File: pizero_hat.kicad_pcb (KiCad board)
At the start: 2 copper layers, 65 x 30 mm, 33 parts, among them J1 Raspberry_Pi_2_3, J2 USB_B_Micro, J3 NEO_6M, J4 MPU6050, J5 JST PH, J6 Conn_01x08_Female, J7 SSD1306, Q1 Si2333CDS, U2 NCP1421

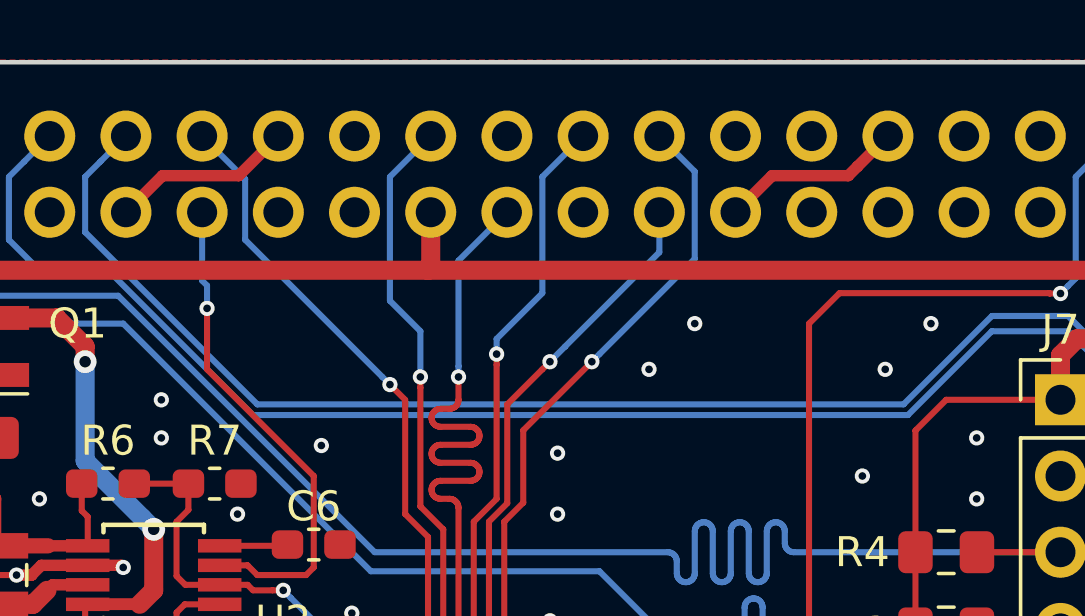
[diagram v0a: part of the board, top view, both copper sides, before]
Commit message: Add Rev A note to silkscreen
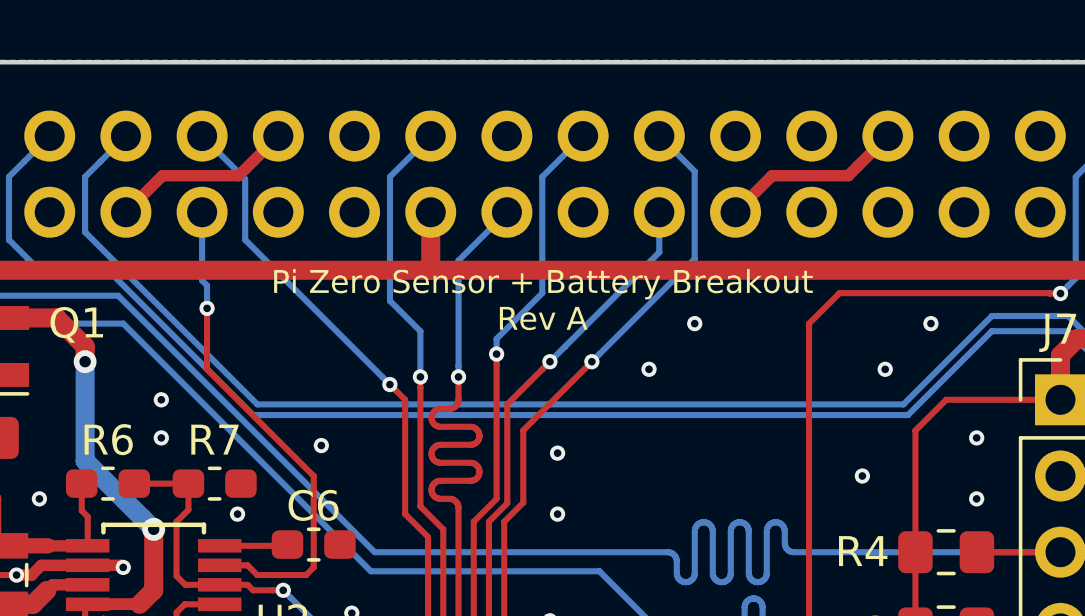
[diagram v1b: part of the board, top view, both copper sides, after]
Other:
- board text added: "Pi Zero Sensor + Battery Breakout Rev A"
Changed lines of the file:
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@@
-(kicad_pcb (version 20171130) (host pcbnew 5.1.4+dfsg1-1)
+(kicad_pcb (version 20171130) (host pcbnew 5.0.2-bee76a0~70~ubuntu18.04.1)
   (general
     (thickness 1.6)
-    (drawings 22)
+    (drawings 23)
     (tracks 580)
     (zones 0)
@@
     (zone_45_only no)
     (trace_min 0.1524)
+    (segment_width 0.2)
+    (edge_width 0.15)
     (via_size 0.508)
     (via_drill 0.254)
@@
     (uvia_min_size 0.2)
     (uvia_min_drill 0.1)
-    (edge_width 0.15)
-    (segment_width 0.2)
     (pcb_text_width 0.3)
     (pcb_text_size 1.5 1.5)
@@
       (net 9 D-))
   )
+  (gr_text "Pi Zero Sensor + Battery Breakout\nRev A" (at 152.4 107.95) (layer F.SilkS)
+    (effects (font (size 0.762 0.762) (thickness 0.127)))
+  )
   (gr_circle (center 123.5 126.5) (end 124.75 126.5) (layer F.Fab) (width 0.2))
